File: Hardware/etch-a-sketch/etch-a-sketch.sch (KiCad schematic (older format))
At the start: 21 parts, among them SW1 Encoder 1, SW2 Encoder 2, U1 LM3671, U2 MCU

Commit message: feat: redo main schematic design
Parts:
- removed C1: 4.7 uF, symbol pspice:CAP
- removed C10: 4.7uF, symbol pspice:CAP
- removed C2: 10 uF, symbol pspice:CAP
- removed C3, C4, C5, C6, C8, C9: 100nF, symbol pspice:CAP
- removed C7: 1uF, symbol pspice:CAP
- removed C?: 0.1uF, symbol pspice:CAP
- removed J?: JTAG, symbol Connector:Conn_ARM_JTAG_SWD_10
- removed L1: 2.2 uH, symbol pspice:INDUCTOR
- removed L2: 22uH, symbol Device:L
- removed R?: 10k, symbol Device:R
- removed SW?: RST, symbol Switch:SW_Push
- removed U1: LM3671, Package_TO_SOT_SMD:TSOT-23-5, symbol Regulator_Switching:LM3670MF
- added C? (x3): 10uF, symbol Device:C_Small
- added C? (x6): 100nF, symbol Device:C_Small
- added C?: 1uF, symbol Device:C_Small
- added C?: 4.7uF, symbol Device:C_Small
- added C? (x2): 12pF, symbol Device:C_Small
- added D?: B5819W, symbol Device:D_Schottky_Small
- added F?: 500mA, symbol Device:Fuse_Small
- added FB? (x2): 100 @ 100MHz, symbol Device:Ferrite_Bead_Small
- added HSE?: 16MHz, symbol Device:Crystal_GND24_Small
- added J?: Conn_02x05_Odd_Even, symbol Connector_Generic:Conn_02x05_Odd_Even
- added R?: 220, symbol Device:R_Small
- added R? (x2): 10k, symbol Device:R_Small
- added U?: AMS1117-3.3, Package_TO_SOT_SMD:SOT-223-3_TabPin2, symbol Regulator_Linear:AMS1117-3.3
- U2: value MCU -> STM32F401RET6
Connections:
- net labels added: +3.3VA, +3V3, BOOT0, BOOT1, HSE_IN, HSE_OUT, SWCLK, SWDIO, SWO
- net labels removed: +3.3V, JTCK_SWCLK, JTDI, JTDO_TRACESWO, JTMS_SWDIO
- wire segments 96 -> 95
- no-connect marks 44 -> 43
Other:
- note added: "Input Voltage Regulator"
- note added: "Resistor and parallel caps\nform a low-pass filter.\n\nAnything above 16MHz can\nbe attenuated."
- note removed: "Always boot to\nmain flash"
- note removed: "Inductor provides additional\nnoise filtration"
- note removed: "Place near VDD and VBAT"
- note removed: "Power Delivery"
- moved on the sheet: SW1, SW2

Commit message: feat: add OLED and encoders
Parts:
- removed DS1: 1_12_mono_oled, symbol 1_12_mono_oled:1_12_mono_oled
- added J2: OLED, symbol Connector:Conn_01x05_Female
- gave numbers to parts that had none: 23
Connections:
- net labels added: ENC1_A, ENC1_B, ENC2_A, ENC2_B, OLED_SCL, OLED_SDA
- net labels removed: 3.3V
- wire segments 95 -> 84
- no-connect marks 43 -> 45
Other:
- moved on the sheet: C10, C11, C12, C13, C3, C4, C5, C6, C7, C8, C9, FB2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

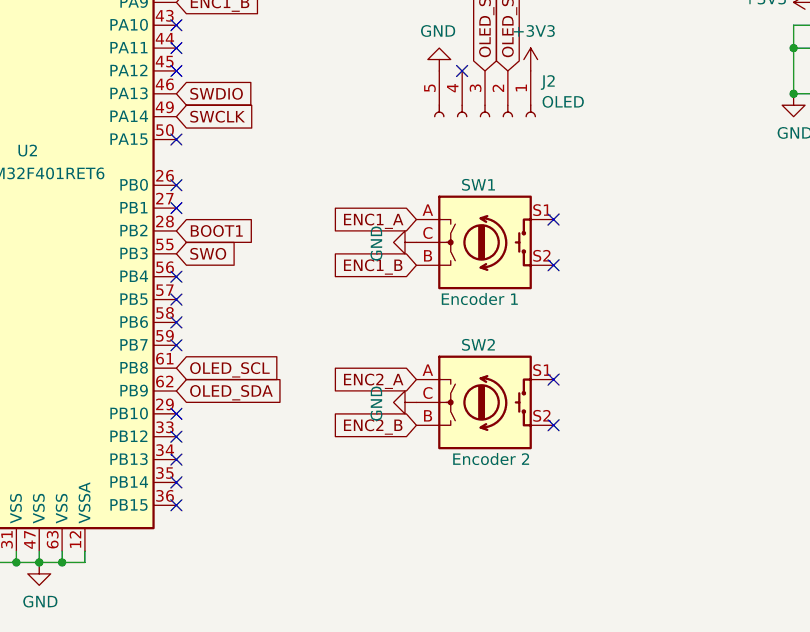
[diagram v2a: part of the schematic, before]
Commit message: feat: add status LED to PB12
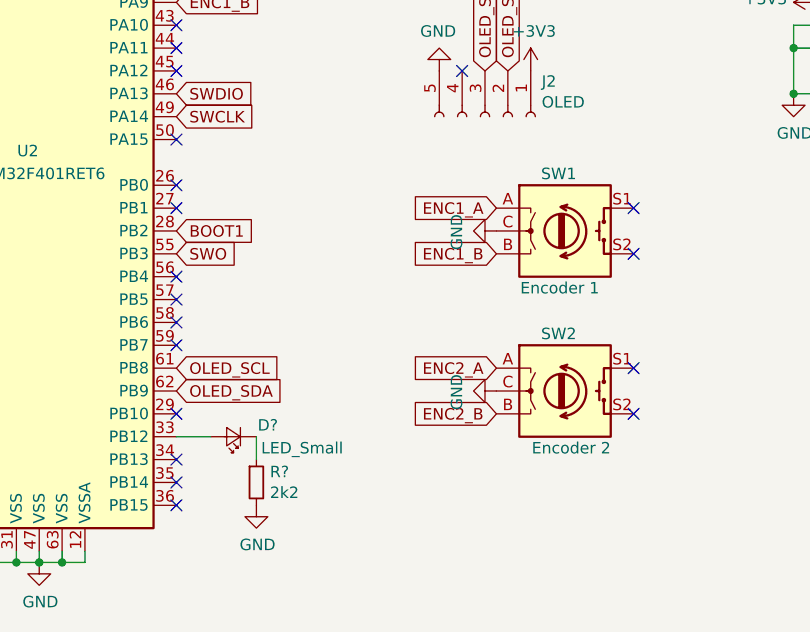
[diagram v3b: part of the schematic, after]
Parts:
- added D?: LED_Small, symbol Device:LED_Small
- added R?: 2k2, symbol Device:R_Small
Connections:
- net GND: now also R?.2
- net at U2.33 (PB12): now also D?.2 (A)
- new net: D?.1 (K), R?.1
- no-connect marks 45 -> 44
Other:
- moved on the sheet: SW1, SW2
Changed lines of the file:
@@
 L Device:Rotary_Encoder_Switch SW1
 U 1 1 5E8A2153
-P 8100 4400
-F 0 "SW1" H 8150 4650 50  0000 R CNN
-F 1 "Encoder 1" H 8250 4150 50  0000 R CNN
-F 2 "" H 7950 4560 50  0001 C CNN
-F 3 "~" H 8100 4660 50  0001 C CNN
-	1    8100 4400
+P 8450 4350
+F 0 "SW1" H 8500 4600 50  0000 R CNN
+F 1 "Encoder 1" H 8600 4100 50  0000 R CNN
+F 2 "" H 8300 4510 50  0001 C CNN
+F 3 "~" H 8450 4610 50  0001 C CNN
+	1    8450 4350
 	1    0    0    -1
 $EndComp
@@
 NoConn ~ 6750 5450
 NoConn ~ 6750 5350
-NoConn ~ 6750 5250
 NoConn ~ 6750 5150
 NoConn ~ 6750 4850
@@
 NoConn ~ 6750 2550
 NoConn ~ 6750 2450
-NoConn ~ 8400 5200
-NoConn ~ 8400 5000
-NoConn ~ 8400 4500
-NoConn ~ 8400 4300
+NoConn ~ 8750 5150
+NoConn ~ 8750 4950
+NoConn ~ 8750 4450
+NoConn ~ 8750 4250
 $Comp
 L power:GND #PWR020
 U 1 1 5E8C8561
-P 7800 4400
-F 0 "#PWR020" H 7800 4150 50  0001 C CNN
-F 1 "GND" H 7805 4227 50  0000 C CNN
-F 2 "" H 7800 4400 50  0001 C CNN
-F 3 "" H 7800 4400 50  0001 C CNN
-	1    7800 4400
+P 8150 4350
+F 0 "#PWR020" H 8150 4100 50  0001 C CNN
+F 1 "GND" H 8155 4177 50  0000 C CNN
+F 2 "" H 8150 4350 50  0001 C CNN
+F 3 "" H 8150 4350 50  0001 C CNN
+	1    8150 4350
 	0    1    1    0
 $EndComp
@@
 L power:GND #PWR021
 U 1 1 5E8C7700
-P 7800 5100
-F 0 "#PWR021" H 7800 4850 50  0001 C CNN
-F 1 "GND" H 7805 4927 50  0000 C CNN
-F 2 "" H 7800 5100 50  0001 C CNN
-F 3 "" H 7800 5100 50  0001 C CNN
-	1    7800 5100
+P 8150 5050
+F 0 "#PWR021" H 8150 4800 50  0001 C CNN
+F 1 "GND" H 8155 4877 50  0000 C CNN
+F 2 "" H 8150 5050 50  0001 C CNN
+F 3 "" H 8150 5050 50  0001 C CNN
+	1    8150 5050
 	0    1    1    0
 $EndComp
@@
 L Device:Rotary_Encoder_Switch SW2
 U 1 1 5E89DE47
-P 8100 5100
-F 0 "SW2" H 8150 5350 50  0000 R CNN
-F 1 "Encoder 2" H 8300 4850 50  0000 R CNN
-F 2 "" H 7950 5260 50  0001 C CNN
-F 3 "~" H 8100 5360 50  0001 C CNN
-	1    8100 5100
+P 8450 5050
+F 0 "SW2" H 8500 5300 50  0000 R CNN
+F 1 "Encoder 2" H 8650 4800 50  0000 R CNN
+F 2 "" H 8300 5210 50  0001 C CNN
+F 3 "~" H 8450 5310 50  0001 C CNN
+	1    8450 5050
 	1    0    0    -1
 $EndComp
@@
 	1    0    0    -1
 $EndComp
-Text GLabel 7800 4300 0    50   Input ~ 0
+Text GLabel 8150 4250 0    50   Input ~ 0
 ENC1_A
-Text GLabel 7800 4500 0    50   Input ~ 0
+Text GLabel 8150 4450 0    50   Input ~ 0
 ENC1_B
-Text GLabel 7800 5200 0    50   Input ~ 0
+Text GLabel 8150 5150 0    50   Input ~ 0
 ENC2_B
-Text GLabel 7800 5000 0    50   Input ~ 0
+Text GLabel 8150 4950 0    50   Input ~ 0
 ENC2_A
 Text GLabel 6750 5050 2    50   Input ~ 0
@@
 NRST
 NoConn ~ 6750 3950
+$Comp
+L Device:LED_Small D?
+U 1 1 5EC7E354
+P 7000 5250
+F 0 "D?" H 6850 5200 50  0000 C CNN
+F 1 "LED_Small" H 6700 5300 50  0000 C CNN
+F 2 "" V 7000 5250 50  0001 C CNN
+F 3 "~" V 7000 5250 50  0001 C CNN
+	1    7000 5250
+	-1   0    0    1
+$EndComp
+Wire Wire Line
+	6750 5250 6900 5250
+$Comp
+L Device:R_Small R?
+U 1 1 5EC81E30
+P 7100 5450
+F 0 "R?" H 7159 5496 50  0000 L CNN
+F 1 "2k2" H 7159 5405 50  0000 L CNN
+F 2 "" H 7100 5450 50  0001 C CNN
+F 3 "~" H 7100 5450 50  0001 C CNN
+	1    7100 5450
+	1    0    0    -1
+$EndComp
+Wire Wire Line
+	7100 5250 7100 5350
+$Comp
+L power:GND #PWR?
+U 1 1 5EC84C86
+P 7100 5550
+F 0 "#PWR?" H 7100 5300 50  0001 C CNN
+F 1 "GND" H 7105 5377 50  0000 C CNN
+F 2 "" H 7100 5550 50  0001 C CNN
+F 3 "" H 7100 5550 50  0001 C CNN
+	1    7100 5550
+	1    0    0    -1
+$EndComp
 $EndSCHEMATC

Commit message: feat: add power LED
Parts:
- added D3: Red, symbol Device:LED_Small
- added R5: 2k2, symbol Device:R_Small
- D2: renamed from D?; value LED_Small -> Red
- gave numbers to parts that had none: 1
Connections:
- net +3V3: now also D3.2 (A)
- net GND: now also R5.2
- new net: D3.1 (K), R5.1
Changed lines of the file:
@@
 Connection ~ 3000 1100
 Wire Notes Line
-	3400 1800 3400 700
+	3700 1800 3700 700
 Wire Notes Line
-	3400 700  650  700
+	3700 700  650  700
 Wire Notes Line
 	650  700  650  1800
 Wire Notes Line
-	650  1800 3400 1800
+	650  1800 3700 1800
 Text Notes 650  650  0    50   ~ 0
 Input Voltage Regulator
@@
 NoConn ~ 6750 3950
 $Comp
-L Device:LED_Small D?
+L Device:LED_Small D2
 U 1 1 5EC7E354
 P 7000 5250
-F 0 "D?" H 6850 5200 50  0000 C CNN
-F 1 "LED_Small" H 6700 5300 50  0000 C CNN
+F 0 "D2" H 6800 5200 50  0000 C CNN
+F 1 "Red" H 6800 5300 50  0000 C CNN
 F 2 "" V 7000 5250 50  0001 C CNN
 F 3 "~" V 7000 5250 50  0001 C CNN
@@
 	6750 5250 6900 5250
 $Comp
-L Device:R_Small R?
+L Device:R_Small R4
 U 1 1 5EC81E30
 P 7100 5450
-F 0 "R?" H 7159 5496 50  0000 L CNN
+F 0 "R4" H 7159 5496 50  0000 L CNN
 F 1 "2k2" H 7159 5405 50  0000 L CNN
 F 2 "" H 7100 5450 50  0001 C CNN
@@
 	7100 5250 7100 5350
 $Comp
-L power:GND #PWR?
+L power:GND #PWR023
 U 1 1 5EC84C86
 P 7100 5550
-F 0 "#PWR?" H 7100 5300 50  0001 C CNN
+F 0 "#PWR023" H 7100 5300 50  0001 C CNN
 F 1 "GND" H 7105 5377 50  0000 C CNN
 F 2 "" H 7100 5550 50  0001 C CNN
@@
 	1    0    0    -1
 $EndComp
+$Comp
+L Device:LED_Small D3
+U 1 1 5EC8B91E
+P 3350 1100
+F 0 "D3" H 3350 895 50  0000 C CNN
+F 1 "Red" H 3350 986 50  0000 C CNN
+F 2 "" V 3350 1100 50  0001 C CNN
+F 3 "~" V 3350 1100 50  0001 C CNN
+	1    3350 1100
+	-1   0    0    1
+$EndComp
+Wire Wire Line
+	3000 1100 3250 1100
+$Comp
+L Device:R_Small R5
+U 1 1 5EC8F1C8
+P 3450 1350
+F 0 "R5" H 3509 1396 50  0000 L CNN
+F 1 "2k2" H 3509 1305 50  0000 L CNN
+F 2 "" H 3450 1350 50  0001 C CNN
+F 3 "~" H 3450 1350 50  0001 C CNN
+	1    3450 1350
+	1    0    0    -1
+$EndComp
+Wire Wire Line
+	3450 1100 3450 1250
+Wire Wire Line
+	3450 1450 3450 1550
+Wire Wire Line
+	3450 1550 3000 1550
+Connection ~ 3000 1550
 $EndSCHEMATC

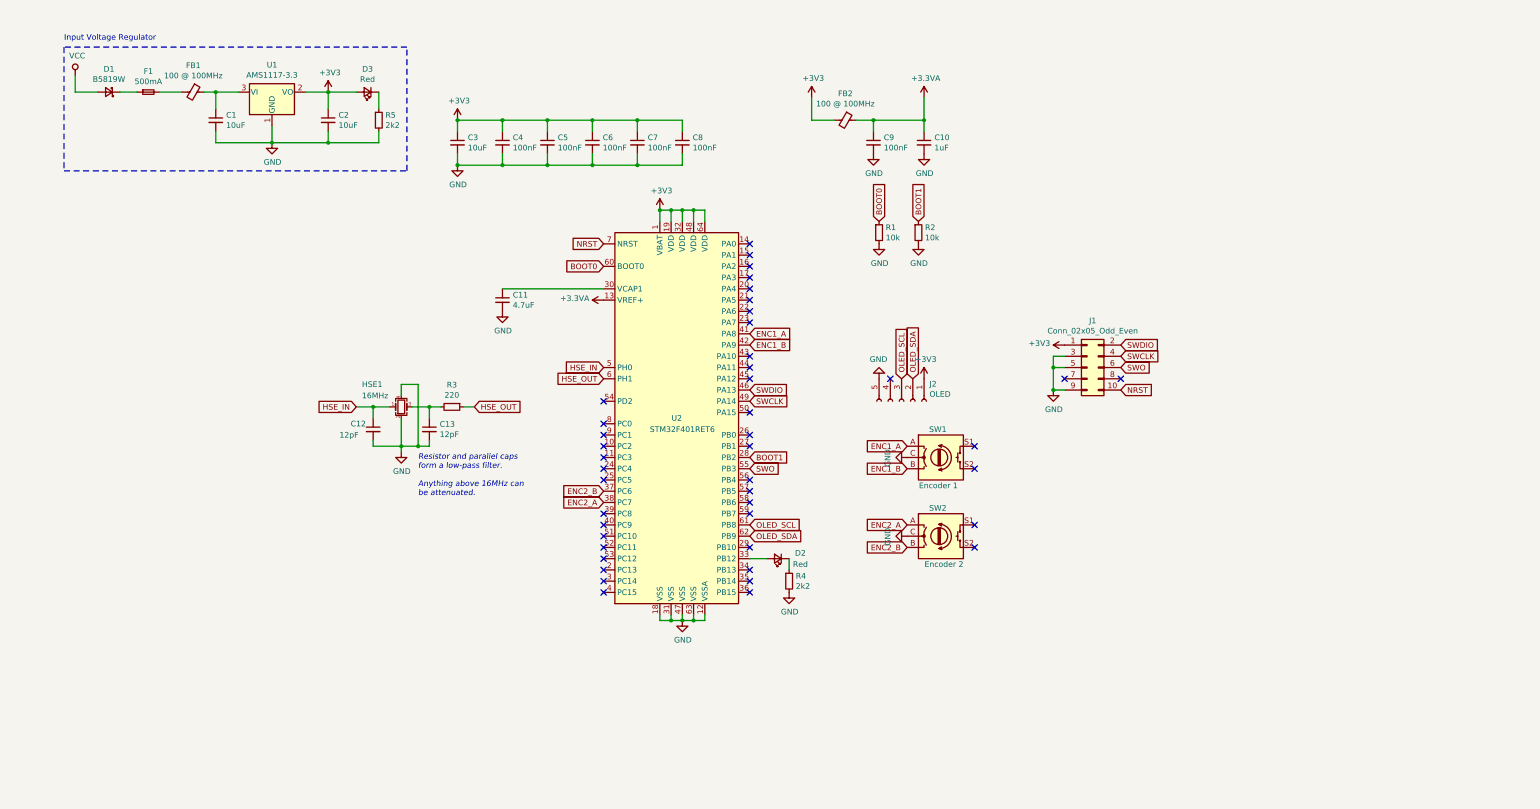
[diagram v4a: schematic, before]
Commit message: feat: organise schematic into blocks
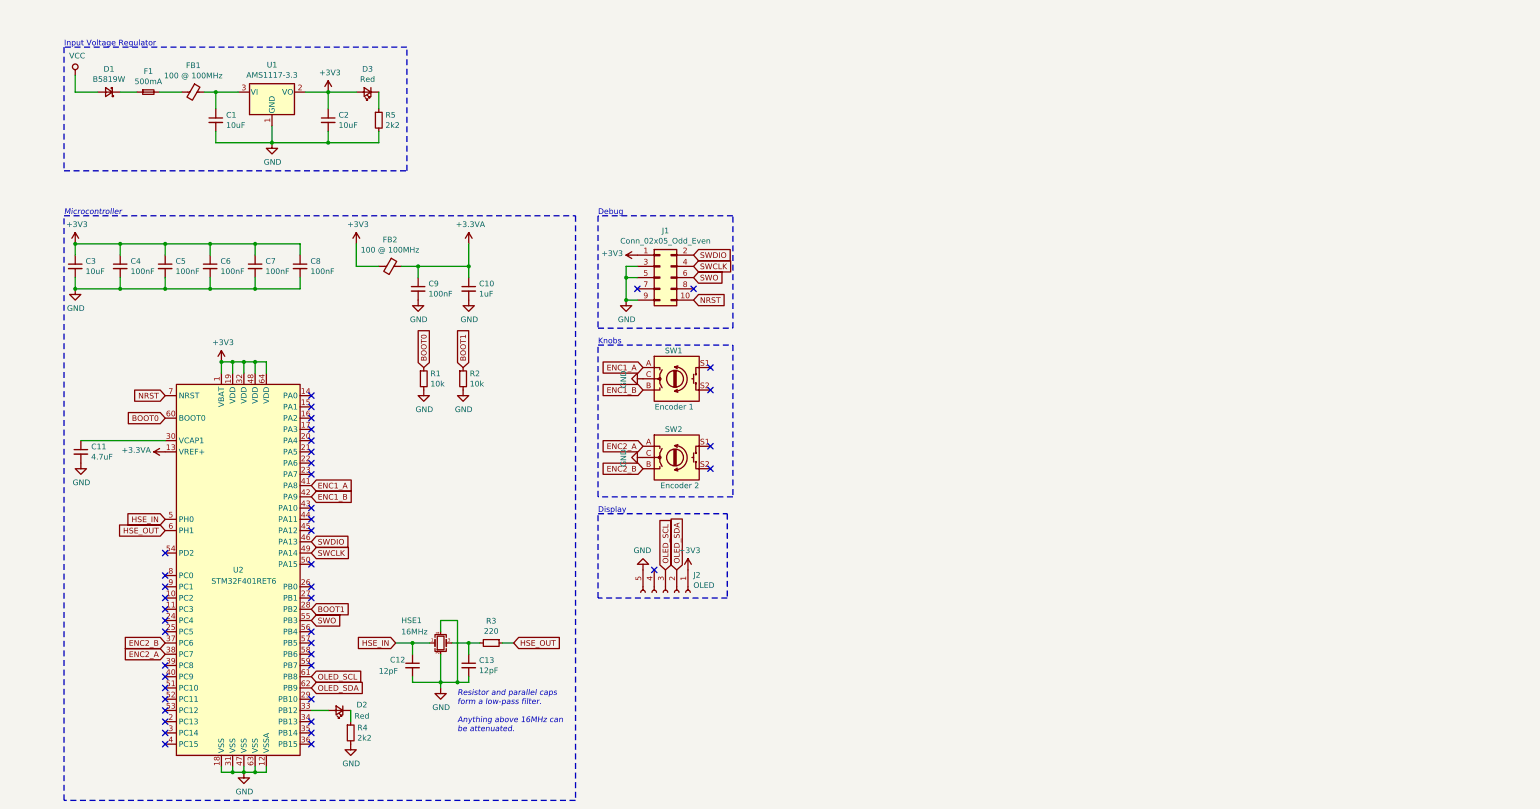
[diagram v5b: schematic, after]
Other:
- note added: "Debug"
- note added: "Display"
- note added: "Knobs"
- note added: "Microcontroller"
- moved on the sheet: C10, C11, C12, C13, C3, C4, C5, C6, C7, C8, C9, D2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

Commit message: feat: add USART to PA2 and PA3, change OLED to generic connector
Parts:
- removed J2: OLED, symbol Connector:Conn_01x05_Female
- added J1: USART, symbol Connector_Generic:Conn_01x02
- added J3: OLED, symbol Connector_Generic:Conn_01x05
- renumbered D3 to D2, D2 to D3, J1 to J2, R5 to R1, R1 to R2, R2 to R3, R3 to R4, R4 to R5
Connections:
- net +3V3: now also J3.1 (Pin_1)
- net GND: now also J3.5 (Pin_5)
- net OLED_SCL: now also J3.3 (Pin_3)
- net OLED_SDA: now also J3.2 (Pin_2)
- net USART2_TX: now reaches U2.16 (PA2)
- net USART2_TX: now also J1.1 (Pin_1)
- net USART2_RX: now reaches U2.17 (PA3)
- net USART2_RX: now also J1.2 (Pin_2)
- no-connect marks 44 -> 42
